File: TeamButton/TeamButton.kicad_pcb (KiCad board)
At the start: 2 copper layers, 79.9 x 70 mm, 5 parts, among them J1 RJ45, SW1 10T85 Microswitch, SW2 10T85 Microswitch

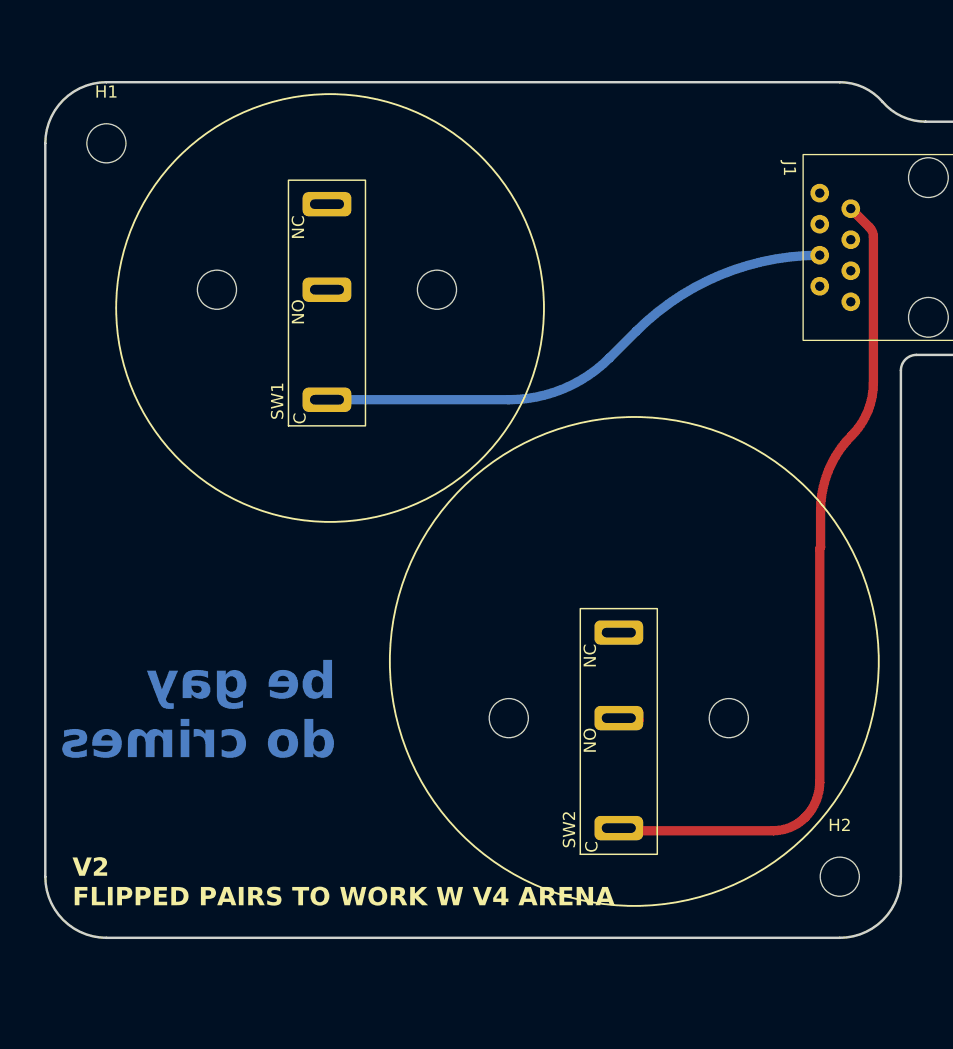
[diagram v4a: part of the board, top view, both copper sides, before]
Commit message: Added visual flourish and confirmed microswitch locations.
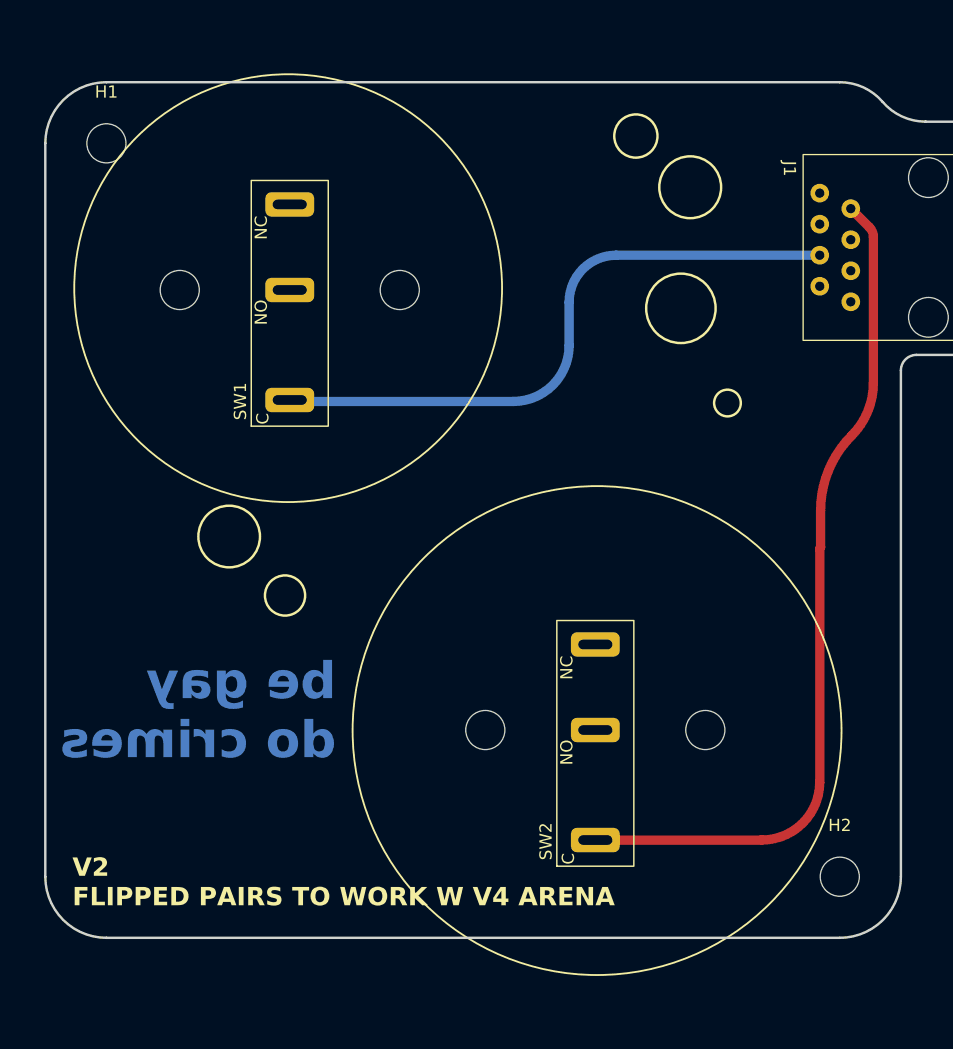
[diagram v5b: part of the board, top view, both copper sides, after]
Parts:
- moved SW1 3.04 mm to (95.0, 62.0)
- moved SW2 2.15 mm to (120.0, 98.0)
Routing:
- net Net-(SW1-C): track 43.6 -> 51.4 mm
- net Net-(SW2-C): track 65.5 -> 69.6 mm
- net GND: track 0.80 -> 0.00 mm
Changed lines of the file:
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@@
   )
   (footprint "footprints:10T85 Microswitch with M3 mounts" (layer "F.Cu")
-    (at 98.044 61.976 90)
+    (at 95 62 90)
     (property "Sheetfile" "TeamButton.kicad_sch")
     (property "Sheetname" "")
@@
   )
   (footprint "footprints:10T85 Microswitch with M3 mounts" (layer "F.Cu")
-    (at 121.92 97.028 90)
+    (at 120 98 90)
     (property "Sheetfile" "TeamButton.kicad_sch")
     (property "Sheetname" "")
@@
     (pad "" np_thru_hole circle (at 0 0) (size 3.2 3.2) (drill 3.2) (layers "*.Cu" "*.Mask"))
   )
-  (gr_circle (center 123.19 92.39) (end 143.19 92.39)
+  (gr_circle (center 90.043 82.169) (end 92.563878 82.169)
+    (stroke (width 0.2) (type default)) (fill none) (layer "F.SilkS"))
+  (gr_circle (center 127.762 53.594) (end 130.292457 53.594)
+    (stroke (width 0.2) (type default)) (fill none) (layer "F.SilkS"))
+  (gr_circle (center 130.81 71.247) (end 131.902495 71.247)
+    (stroke (width 0.2) (type default)) (fill none) (layer "F.SilkS"))
+  (gr_circle (center 120.142 98.044) (end 140.142 98.044)
     (stroke (width 0.15) (type default)) (fill none) (layer "F.SilkS"))
-  (gr_circle (center 98.298 63.474) (end 115.798 63.474)
+  (gr_circle (center 94.615 86.995) (end 96.139 87.610878)
+    (stroke (width 0.2) (type default)) (fill none) (layer "F.SilkS"))
+  (gr_circle (center 94.869 61.849) (end 112.369 61.849)
     (stroke (width 0.15) (type default)) (fill none) (layer "F.SilkS"))
+  (gr_circle (center 123.317 49.403) (end 125.085905 49.403)
+    (stroke (width 0.2) (type default)) (fill none) (layer "F.SilkS"))
+  (gr_circle (center 127 63.5) (end 129.839806 63.5)
+    (stroke (width 0.2) (type default)) (fill none) (layer "F.SilkS"))
+  (gr_circle (center 112.014 49.657) (end 113.741387 49.657)
+    (stroke (width 0.2) (type default)) (fill none) (layer "F.Mask"))
+  (gr_circle (center 124.333 72.644) (end 127.121221 72.644)
+    (stroke (width 0.2) (type default)) (fill none) (layer "F.Mask"))
+  (gr_circle (center 97.536 81.915) (end 99.825525 81.915)
+    (stroke (width 0.2) (type default)) (fill none) (layer "F.Mask"))
   (gr_line (start 154.94 67.31) (end 154.94 48.227746)
     (stroke (width 0.1) (type default)) (layer "Edge.Cuts"))
@@
     (effects (font (size 1.5 1.5) (thickness 0.3) bold) (justify left bottom))
   )
-  (segment (start 123.825 97.155) (end 123.825 97.24) (width 0.25) (layer "F.Cu") (net 1))
-  (segment (start 123.825 97.24) (end 123.825 96.52) (width 0.25) (layer "F.Cu") (net 1))
-  (segment (start 140.9 55.345) (end 142.420596 56.865596) (width 0.762) (layer "F.Cu") (net 6))
+  (segment (start 142.748 69.621529) (end 142.748 57.656019) (width 0.762) (layer "F.Cu") (net 6))
+  (segment (start 120 107) (end 133.618944 107) (width 0.762) (layer "F.Cu") (net 6))
+  (segment (start 138.36 102.258944) (end 138.36 83.226994) (width 0.762) (layer "F.Cu") (net 6))
   (segment (start 138.43 83.058) (end 138.43 80.046102) (width 0.762) (layer "F.Cu") (net 6))
-  (segment (start 142.748 69.621529) (end 142.748 57.656019) (width 0.762) (layer "F.Cu") (net 6))
-  (segment (start 123.825 106.24) (end 134.542993 106.24) (width 0.762) (layer "F.Cu") (net 6))
-  (segment (start 138.36 102.258944) (end 138.36 83.226994) (width 0.762) (layer "F.Cu") (net 6))
-  (arc (start 134.542993 106.24) (mid 135.959307 105.958278) (end 137.16 105.156) (width 0.762) (layer "F.Cu") (net 6))
-  (arc (start 137.16 105.156) (mid 138.04813 103.826819) (end 138.36 102.258944) (width 0.762) (layer "F.Cu") (net 6))
+  (segment (start 142.420596 56.865596) (end 140.9 55.345) (width 0.762) (layer "F.Cu") (net 6))
   (arc (start 138.43 80.046102) (mid 139.090125 76.727433) (end 140.97 73.914) (width 0.762) (layer "F.Cu") (net 6))
+  (arc (start 138.36 83.226994) (mid 138.378193 83.135536) (end 138.43 83.058) (width 0.762) (layer "F.Cu") (net 6))
   (arc (start 142.748 57.656019) (mid 142.66291 57.228245) (end 142.420596 56.865596) (width 0.762) (layer "F.Cu") (net 6))
+  (arc (start 133.618944 107) (mid 136.971377 105.611377) (end 138.36 102.258944) (width 0.762) (layer "F.Cu") (net 6))
   (arc (start 140.97 73.914) (mid 142.285913 71.944598) (end 142.748 69.621529) (width 0.762) (layer "F.Cu") (net 6))
-  (arc (start 138.36 83.226994) (mid 138.378193 83.135536) (end 138.43 83.058) (width 0.762) (layer "F.Cu") (net 6))
-  (segment (start 121.158 67.564) (end 123.349409 65.372591) (width 0.762) (layer "B.Cu") (net 8))
-  (segment (start 98.044 70.976) (end 112.920704 70.976) (width 0.762) (layer "B.Cu") (net 8))
-  (arc (start 123.349409 65.372591) (mid 130.236326 60.7709) (end 138.36 59.155) (width 0.762) (layer "B.Cu") (net 8))
-  (arc (start 112.920704 70.976) (mid 117.378696 70.08925) (end 121.158 67.564) (width 0.762) (layer "B.Cu") (net 8))
+  (segment (start 138.36 59.155) (end 121.693 59.155) (width 0.762) (layer "B.Cu") (net 8))
+  (segment (start 117.856 62.992) (end 117.856 66.548) (width 0.762) (layer "B.Cu") (net 8))
+  (segment (start 113.284 71.12) (end 95.12 71.12) (width 0.762) (layer "B.Cu") (net 8))
+  (arc (start 121.693 59.155) (mid 118.979831 60.278831) (end 117.856 62.992) (width 0.762) (layer "B.Cu") (net 8))
+  (arc (start 95.12 71.12) (mid 95.035147 71.084853) (end 95 71) (width 0.762) (layer "B.Cu") (net 8))
+  (arc (start 117.856 66.548) (mid 116.516892 69.780892) (end 113.284 71.12) (width 0.762) (layer "B.Cu") (net 8))
   (zone (net 1) (net_name "GND") (layers "F&B.Cu") (name "GND") (hatch edge 0.508)
     (connect_pads (clearance 0.508))

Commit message: Same deal.
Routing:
- net Net-(SW2-C): track 69.6 -> 70.8 mm
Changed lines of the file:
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@@
   (gr_circle (center 94.615 86.995) (end 96.139 87.610878)
     (stroke (width 0.2) (type default)) (fill none) (layer "F.SilkS"))
-  (gr_circle (center 94.869 61.849) (end 112.369 61.849)
+  (gr_circle (center 94.869 61.849) (end 111.887 61.849)
     (stroke (width 0.15) (type default)) (fill none) (layer "F.SilkS"))
   (gr_circle (center 123.317 49.403) (end 125.085905 49.403)
@@
     (effects (font (size 1.5 1.5) (thickness 0.3) bold) (justify left bottom))
   )
-  (segment (start 142.748 69.621529) (end 142.748 57.656019) (width 0.762) (layer "F.Cu") (net 6))
-  (segment (start 120 107) (end 133.618944 107) (width 0.762) (layer "F.Cu") (net 6))
-  (segment (start 138.36 102.258944) (end 138.36 83.226994) (width 0.762) (layer "F.Cu") (net 6))
-  (segment (start 138.43 83.058) (end 138.43 80.046102) (width 0.762) (layer "F.Cu") (net 6))
-  (segment (start 142.420596 56.865596) (end 140.9 55.345) (width 0.762) (layer "F.Cu") (net 6))
-  (arc (start 138.43 80.046102) (mid 139.090125 76.727433) (end 140.97 73.914) (width 0.762) (layer "F.Cu") (net 6))
-  (arc (start 138.36 83.226994) (mid 138.378193 83.135536) (end 138.43 83.058) (width 0.762) (layer "F.Cu") (net 6))
-  (arc (start 142.748 57.656019) (mid 142.66291 57.228245) (end 142.420596 56.865596) (width 0.762) (layer "F.Cu") (net 6))
-  (arc (start 133.618944 107) (mid 136.971377 105.611377) (end 138.36 102.258944) (width 0.762) (layer "F.Cu") (net 6))
-  (arc (start 140.97 73.914) (mid 142.285913 71.944598) (end 142.748 69.621529) (width 0.762) (layer "F.Cu") (net 6))
+  (segment (start 133.618944 107) (end 120 107) (width 0.762) (layer "F.Cu") (net 6))
+  (segment (start 140.9 55.345) (end 142.420596 56.865596) (width 0.762) (layer "F.Cu") (net 6))
+  (segment (start 138.36 76.524) (end 138.36 102.258944) (width 0.762) (layer "F.Cu") (net 6))
+  (segment (start 142.748 57.656019) (end 142.748 72.136) (width 0.762) (layer "F.Cu") (net 6))
+  (arc (start 142.748 72.136) (mid 142.227236 73.393236) (end 140.97 73.914) (width 0.762) (layer "F.Cu") (net 6))
+  (arc (start 140.97 73.914) (mid 139.124451 74.678451) (end 138.36 76.524) (width 0.762) (layer "F.Cu") (net 6))
+  (arc (start 138.36 102.258944) (mid 136.971377 105.611377) (end 133.618944 107) (width 0.762) (layer "F.Cu") (net 6))
+  (arc (start 142.420596 56.865596) (mid 142.66291 57.228245) (end 142.748 57.656019) (width 0.762) (layer "F.Cu") (net 6))
   (segment (start 138.36 59.155) (end 121.693 59.155) (width 0.762) (layer "B.Cu") (net 8))
   (segment (start 117.856 62.992) (end 117.856 66.548) (width 0.762) (layer "B.Cu") (net 8))

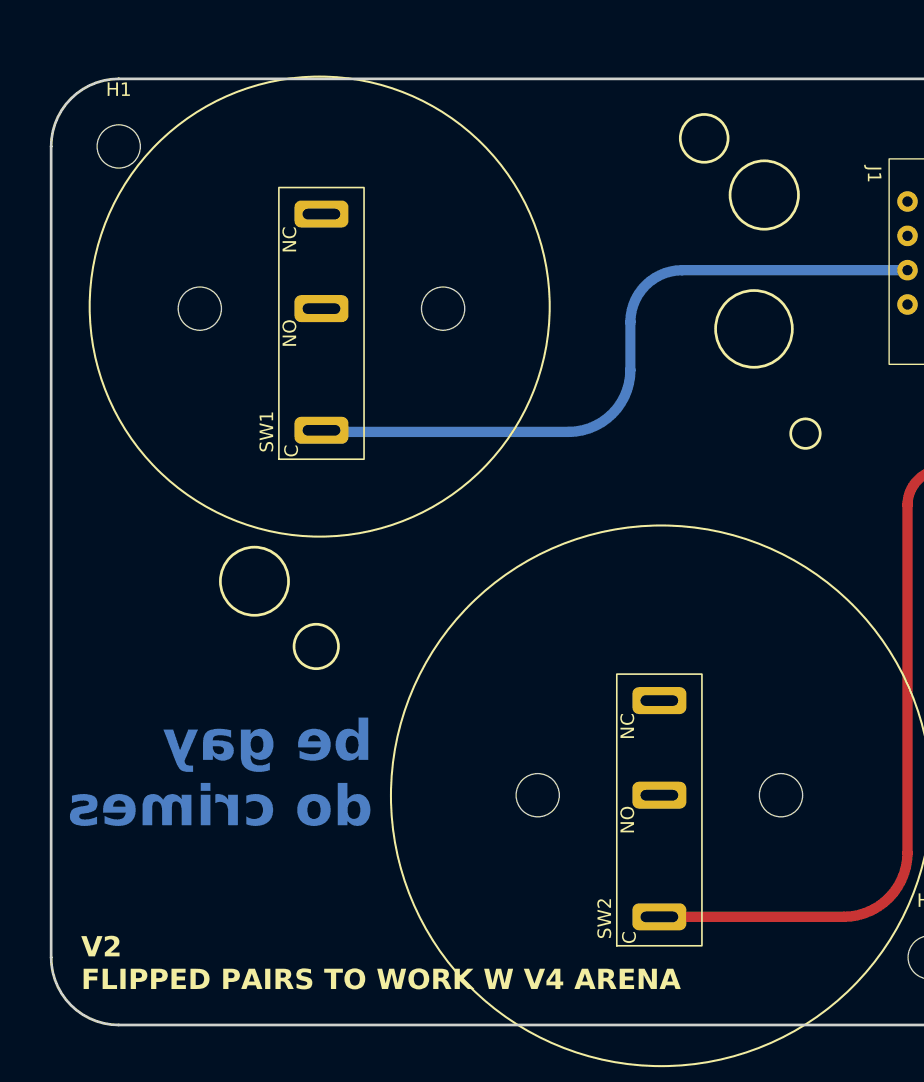
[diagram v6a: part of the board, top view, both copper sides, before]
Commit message: Added reset pins back in and broke out the pins in the team control area; should be easier now.  Yay!
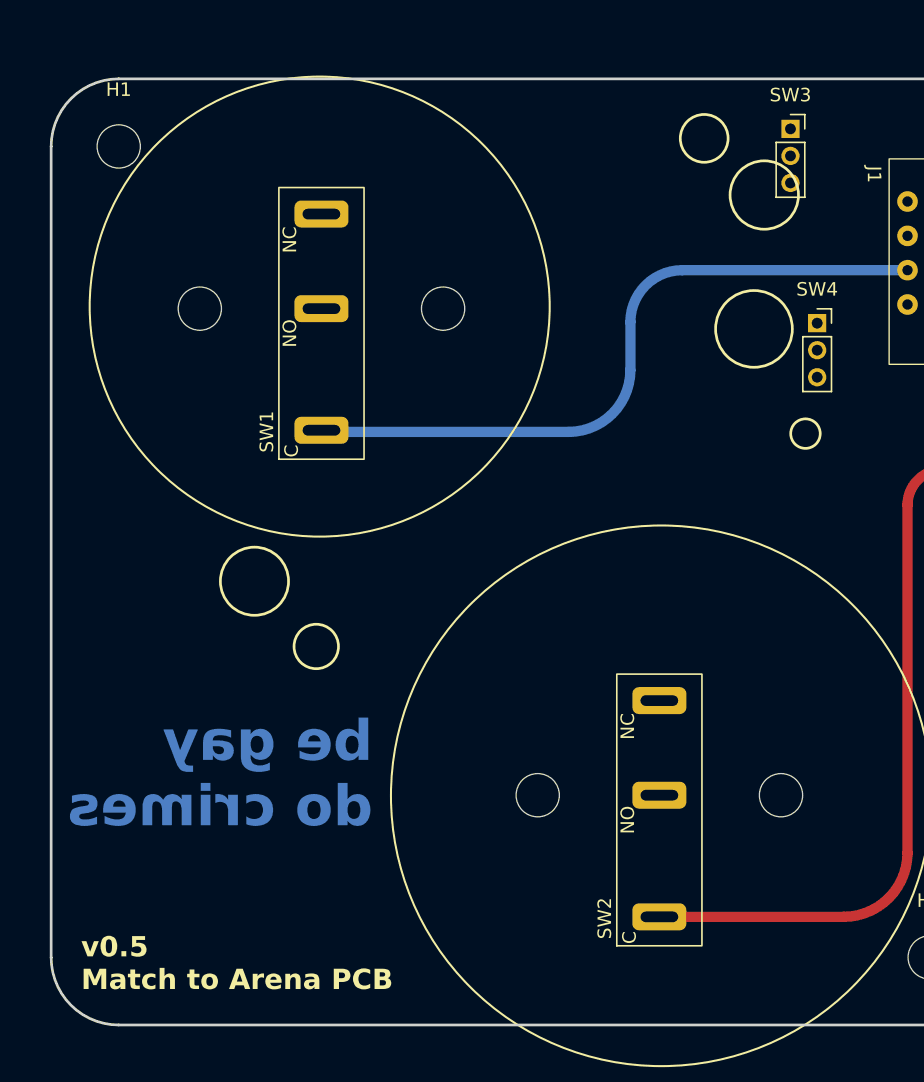
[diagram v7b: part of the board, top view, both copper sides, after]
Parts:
- added SW3: ~, Connector_PinSocket_2.00mm:PinSocket_1x03_P2.00mm_Vertical, F.Cu at (129.7, 48.7)
- added SW4: ~, Connector_PinSocket_2.00mm:PinSocket_1x03_P2.00mm_Vertical, F.Cu at (131.7, 63.1)
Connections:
- net Net-(SW1-C) renamed /P_START
- net Net-(SW2-C) renamed /P_END
- J1 pad 5: unconnected-(J1-Pad5) -> /P_RST
- J1 pad 6: unconnected-(J1-Pad6) -> /P_PAUSE
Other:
- board text added: "END!"
- board text added: "PAUSE"
- board text added: "RESET"
- board text added: "START!"
- board text added: "v0.5 Match to Arena PCB"
- board text removed: "V2 FLIPPED PAIRS TO WORK W V4 ARENA"

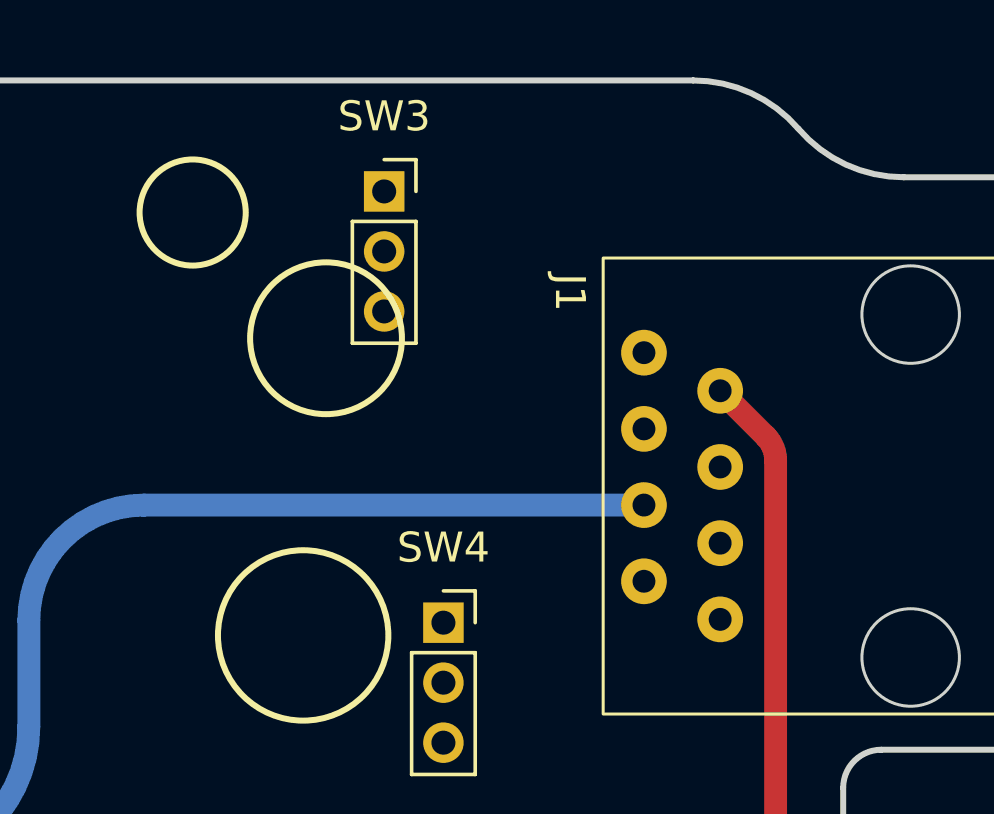
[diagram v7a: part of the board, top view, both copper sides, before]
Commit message: Updated PCB revisions, swapped to larger footprint for stacklight connector, release cutting soon.
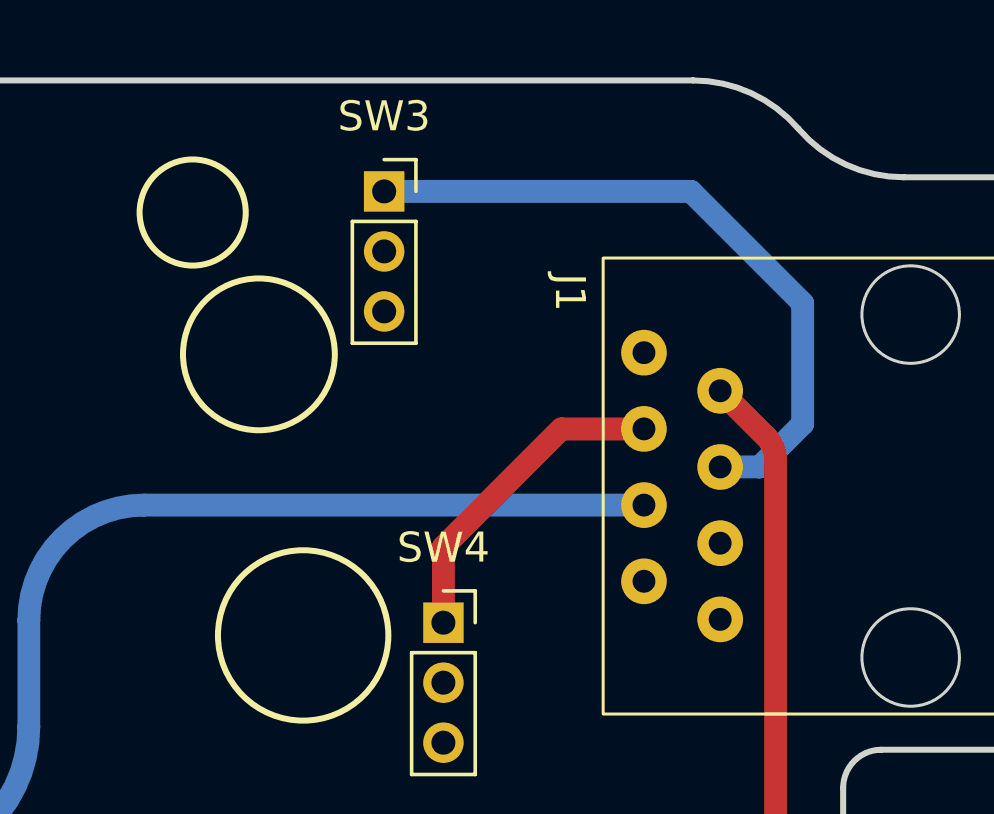
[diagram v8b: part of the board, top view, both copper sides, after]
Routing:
- net /P_RST: track 0.00 -> 22.9 mm
- net /P_PAUSE: track 0.00 -> 10.8 mm
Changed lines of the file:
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@@
   (gr_circle (center 90.043 82.169) (end 92.563878 82.169)
     (stroke (width 0.2) (type default)) (fill none) (layer "F.SilkS"))
-  (gr_circle (center 127.762 53.594) (end 130.292457 53.594)
+  (gr_circle (center 125.525 54.130457) (end 128.055457 54.130457)
     (stroke (width 0.2) (type default)) (fill none) (layer "F.SilkS"))
   (gr_circle (center 130.81 71.247) (end 131.902495 71.247)
@@
   (arc (start 95.12 71.12) (mid 95.035147 71.084853) (end 95 71) (width 0.762) (layer "B.Cu") (net 4))
   (arc (start 117.856 66.548) (mid 116.516892 69.780892) (end 113.284 71.12) (width 0.762) (layer "B.Cu") (net 4))
+  (segment (start 142.215 57.885) (end 143.65 56.45) (width 0.762) (layer "B.Cu") (net 6))
+  (segment (start 143.65 52.425) (end 139.925 48.7) (width 0.762) (layer "B.Cu") (net 6))
+  (segment (start 139.925 48.7) (end 129.7 48.7) (width 0.762) (layer "B.Cu") (net 6))
+  (segment (start 143.65 56.45) (end 143.65 52.425) (width 0.762) (layer "B.Cu") (net 6))
+  (segment (start 140.9 57.885) (end 142.215 57.885) (width 0.762) (layer "B.Cu") (net 6))
+  (segment (start 131.675 60.55) (end 135.61 56.615) (width 0.762) (layer "F.Cu") (net 7))
+  (segment (start 135.61 56.615) (end 138.36 56.615) (width 0.762) (layer "F.Cu") (net 7))
+  (segment (start 131.675 63.075) (end 131.675 60.55) (width 0.762) (layer "F.Cu") (net 7))
   (segment (start 133.618944 107) (end 120 107) (width 0.762) (layer "F.Cu") (net 8))
   (segment (start 140.9 55.345) (end 142.420596 56.865596) (width 0.762) (layer "F.Cu") (net 8))
